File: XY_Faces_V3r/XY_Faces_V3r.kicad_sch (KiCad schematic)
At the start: 33 parts, among them CN1 DF11-2DSA-4DP, J2 Conn_01x01, J3 Conn_01x01, J4 Conn_01x01, J5 Conn_01x01, U1 VEML7700, U2 TMP112xxDRL, U3 DRV2605LDGS, U4 TCA4311ADGKR, U5 5040500691, U6 5040500691

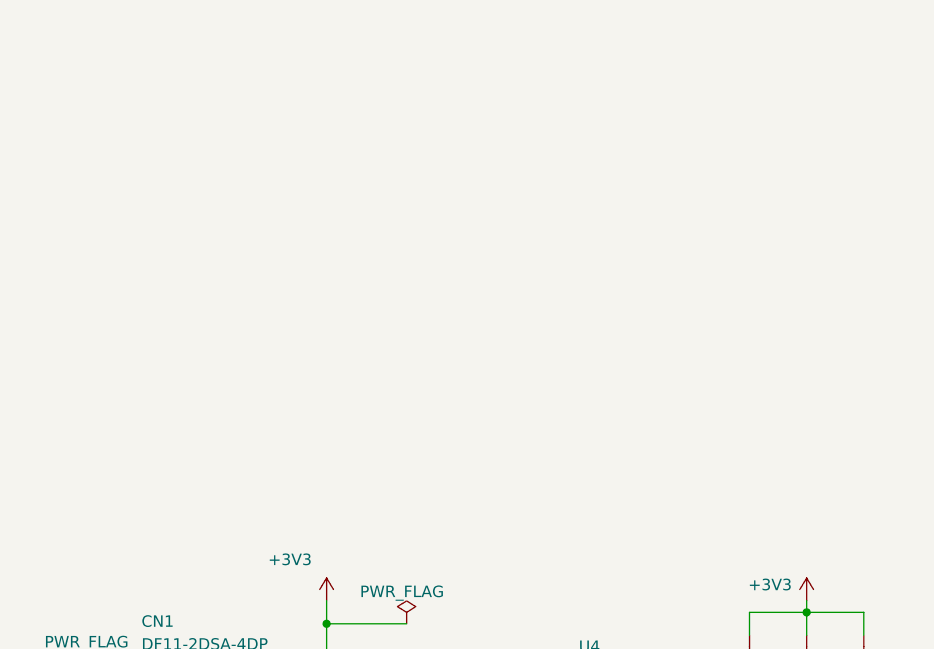
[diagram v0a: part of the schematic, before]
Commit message: Changed all Passives to 0402
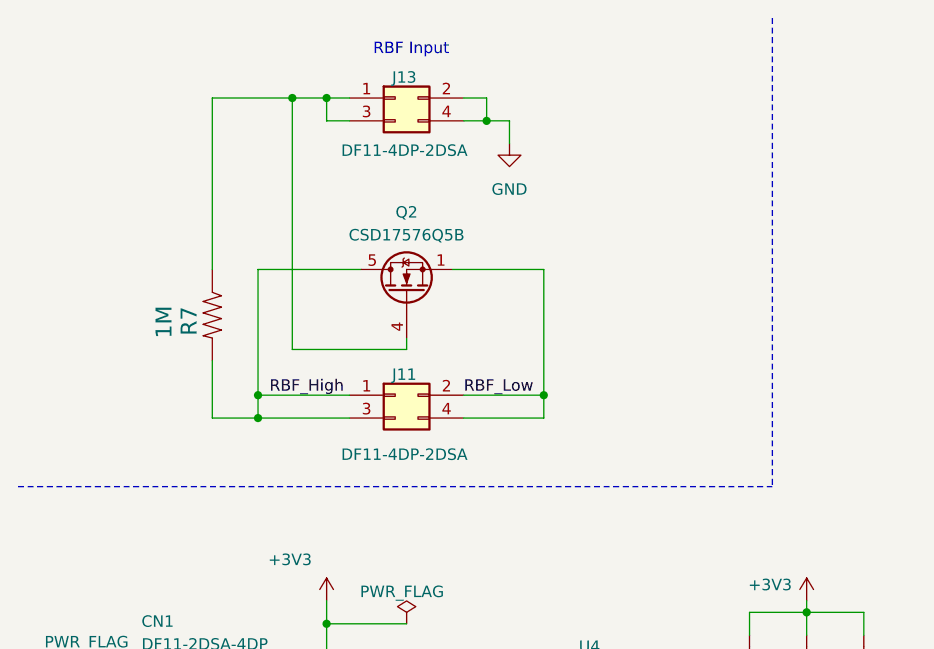
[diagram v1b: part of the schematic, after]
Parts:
- added J11, J13: DF11-4DP-2DSA, Connector_Hirose:Hirose_DF11-4DP-2DSA_2x02_P2.00mm_Vertical, symbol Connector_Generic:Conn_02x02_Odd_Even
- added Q2: CSD17576Q5B, Package_TO_SOT_SMD:TDSON-8-1, symbol Transistor_FET:CSD17576Q5B
- added R7: 1M, Resistor_SMD:R_0603_1608Metric, symbol mainboard:RESISTOR0603
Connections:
- net GND: now also J13.2 (Pin_2), J13.4 (Pin_4)
- new net: J13.1 (Pin_1), J13.3 (Pin_3), Q2.4 (G), R7.1
- new net RBF_High: J11.1 (Pin_1), J11.3 (Pin_3), Q2.5 (D), R7.2
- new net RBF_Low: J11.2 (Pin_2), J11.4 (Pin_4), Q2.1 (S), Q2.2 (S), Q2.3 (S)
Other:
- note added: "RBF Input"
